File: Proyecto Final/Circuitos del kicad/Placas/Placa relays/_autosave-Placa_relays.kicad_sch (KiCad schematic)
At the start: 23 parts, among them J1 Conn_02x05_Odd_Even, Q1 PN2222A, Q2 PN2222A, Q3 PN2222A

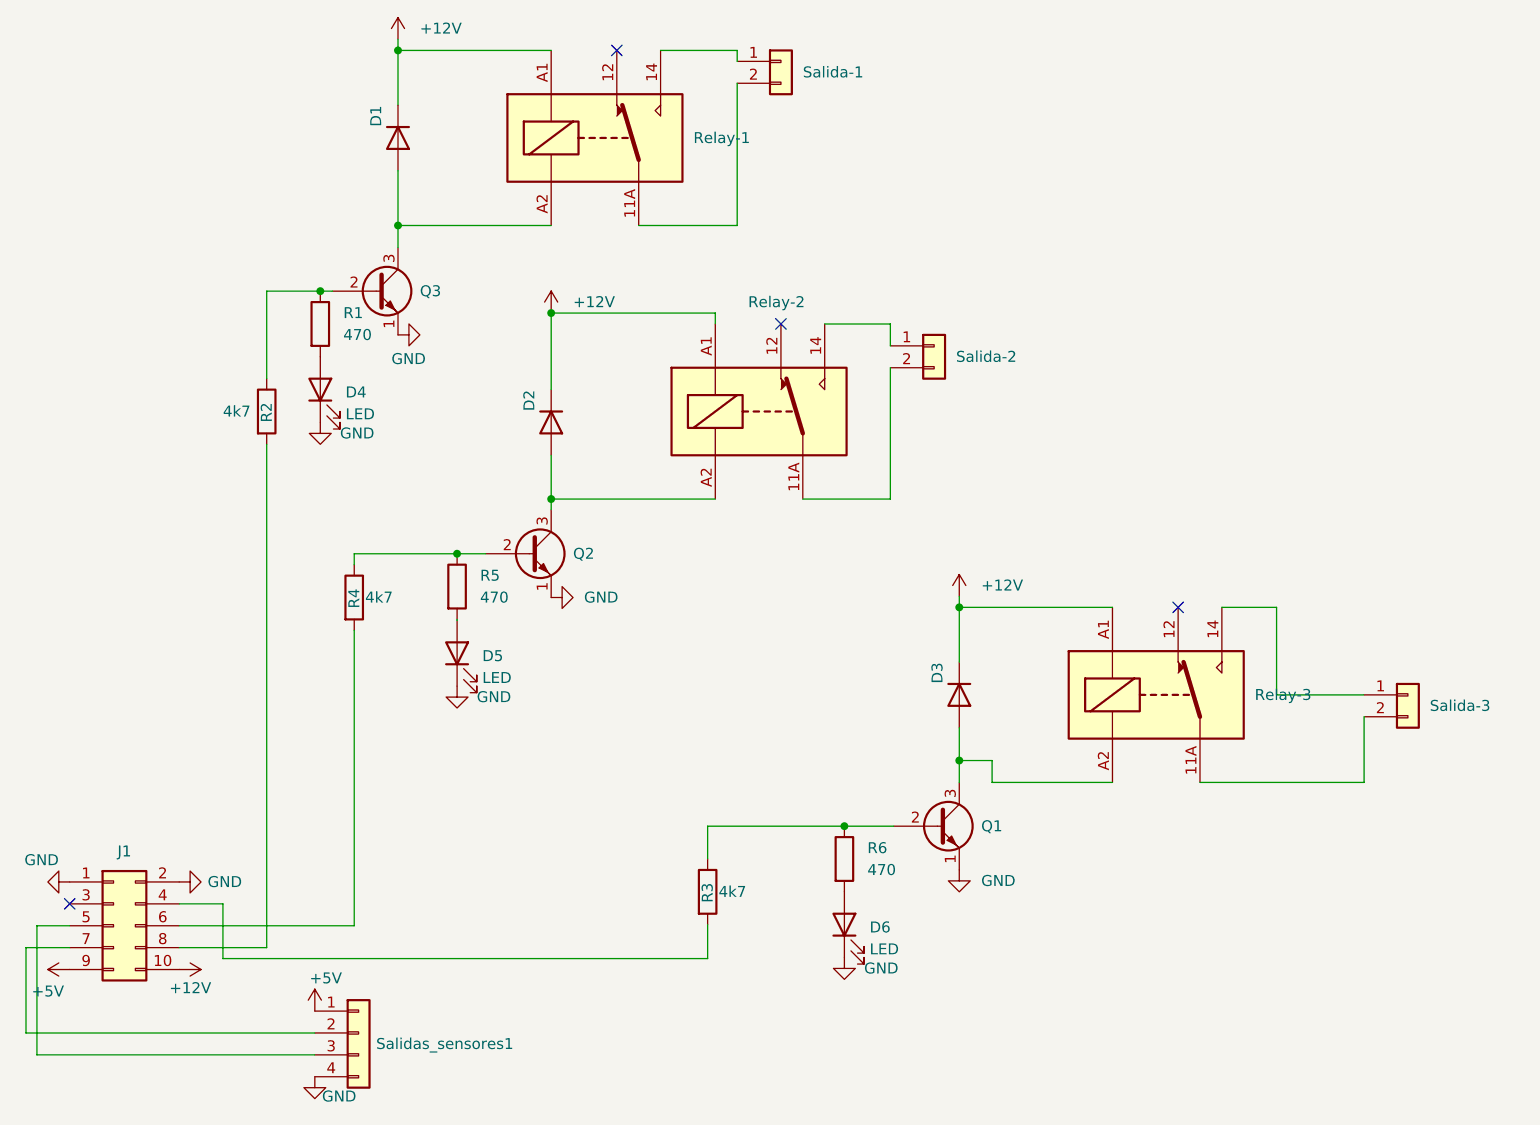
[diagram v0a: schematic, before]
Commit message: Agregado placa todo en uno
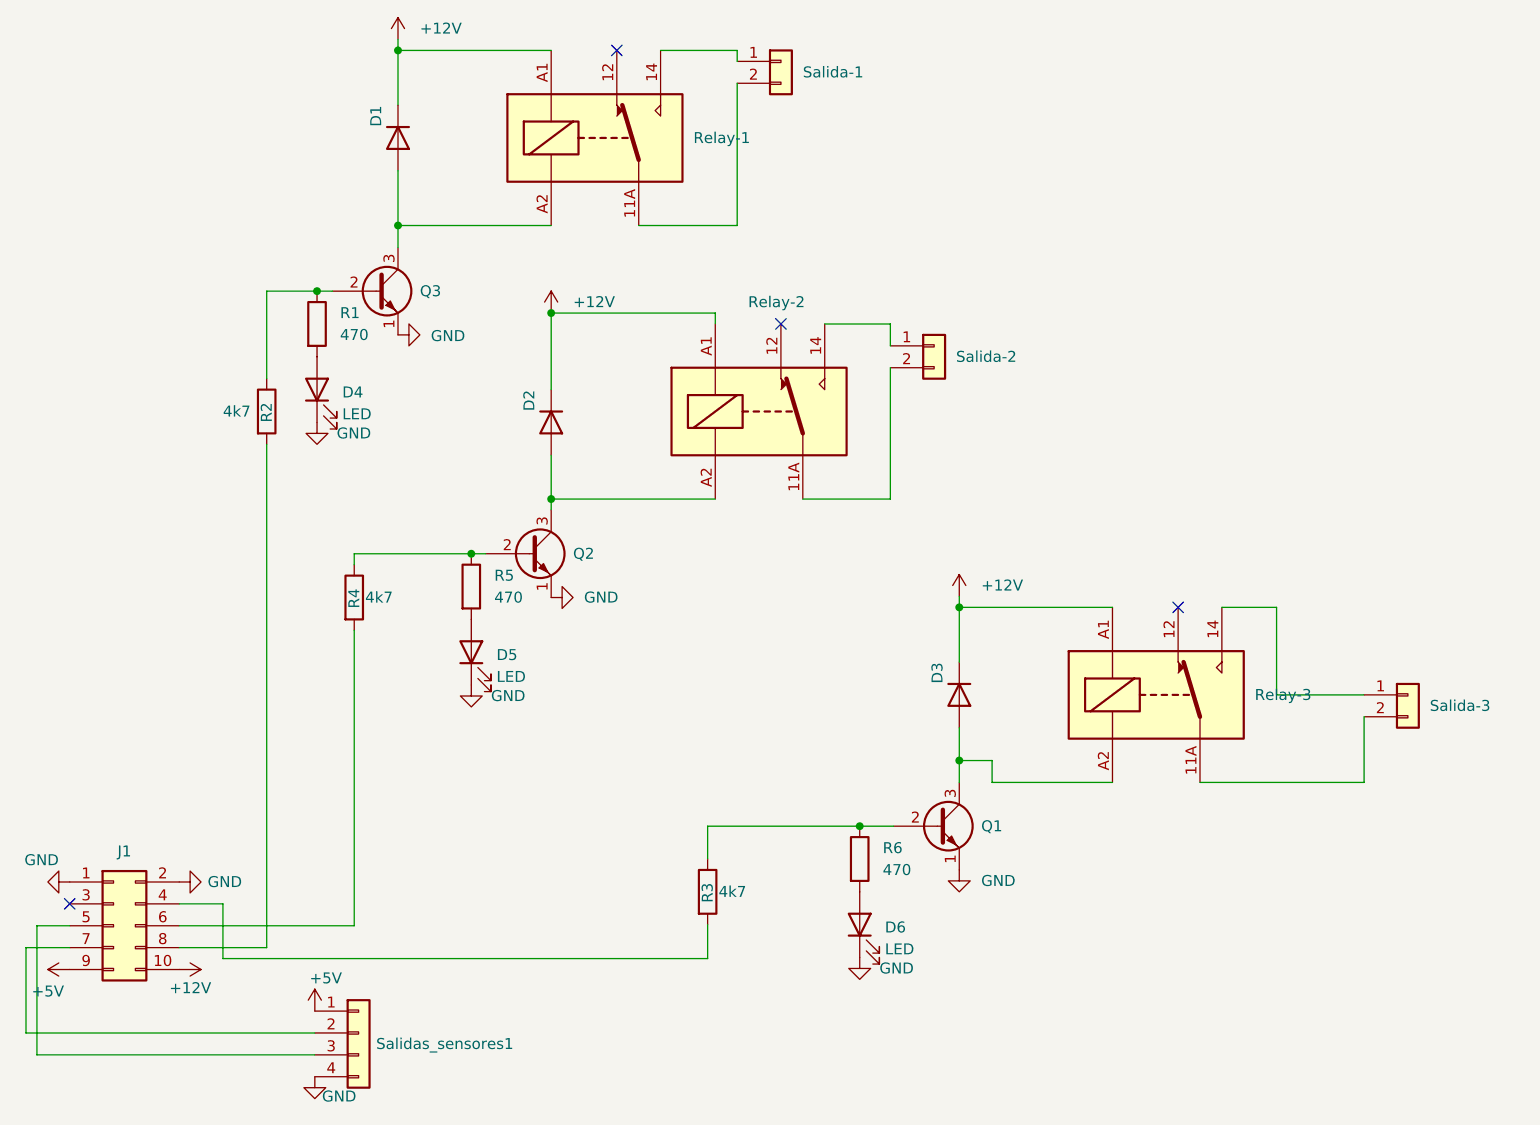
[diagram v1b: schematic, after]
